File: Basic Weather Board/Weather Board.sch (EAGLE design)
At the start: 4 parts, among them U1 AT30TS75, U2 TMP101", U3 LPS331AP, U4 MPL3115A2

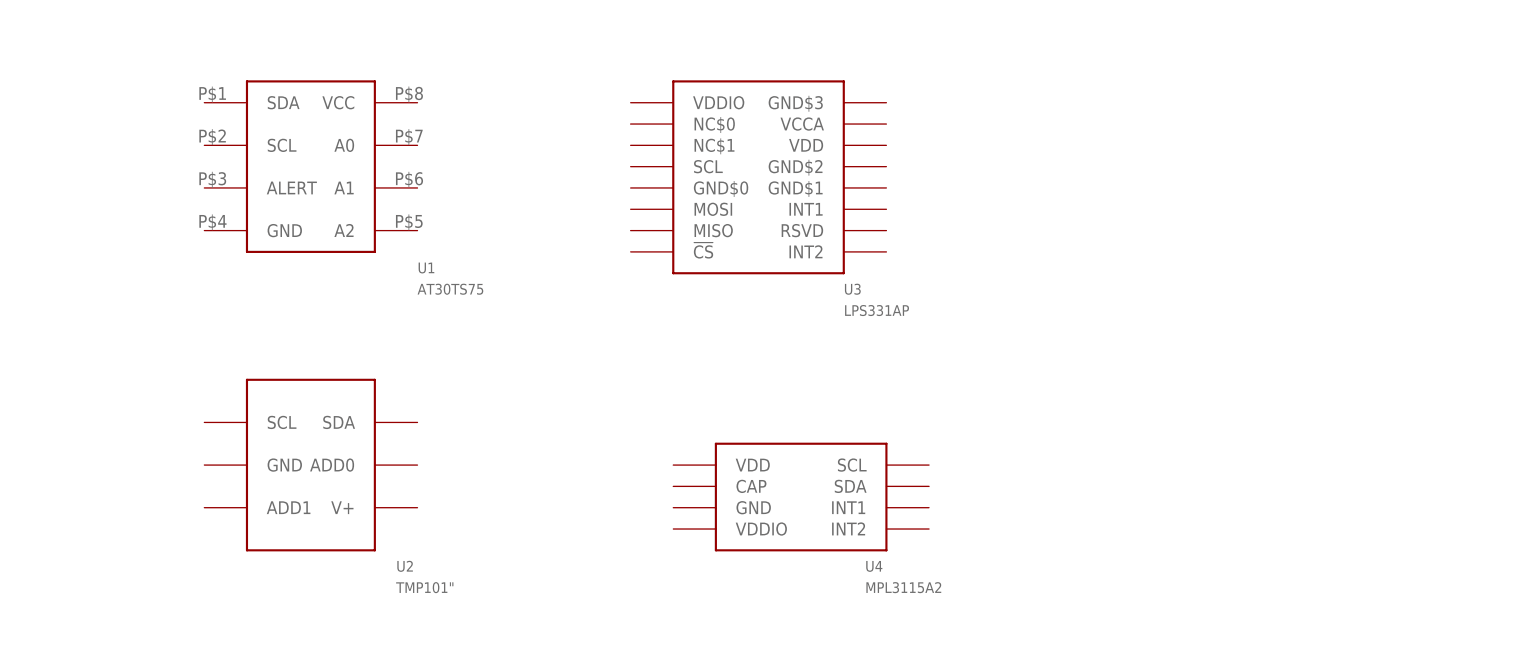
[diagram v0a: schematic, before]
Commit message: FRDM-KL25Z: Corrected parts to use Newark approved components and added missing componnets
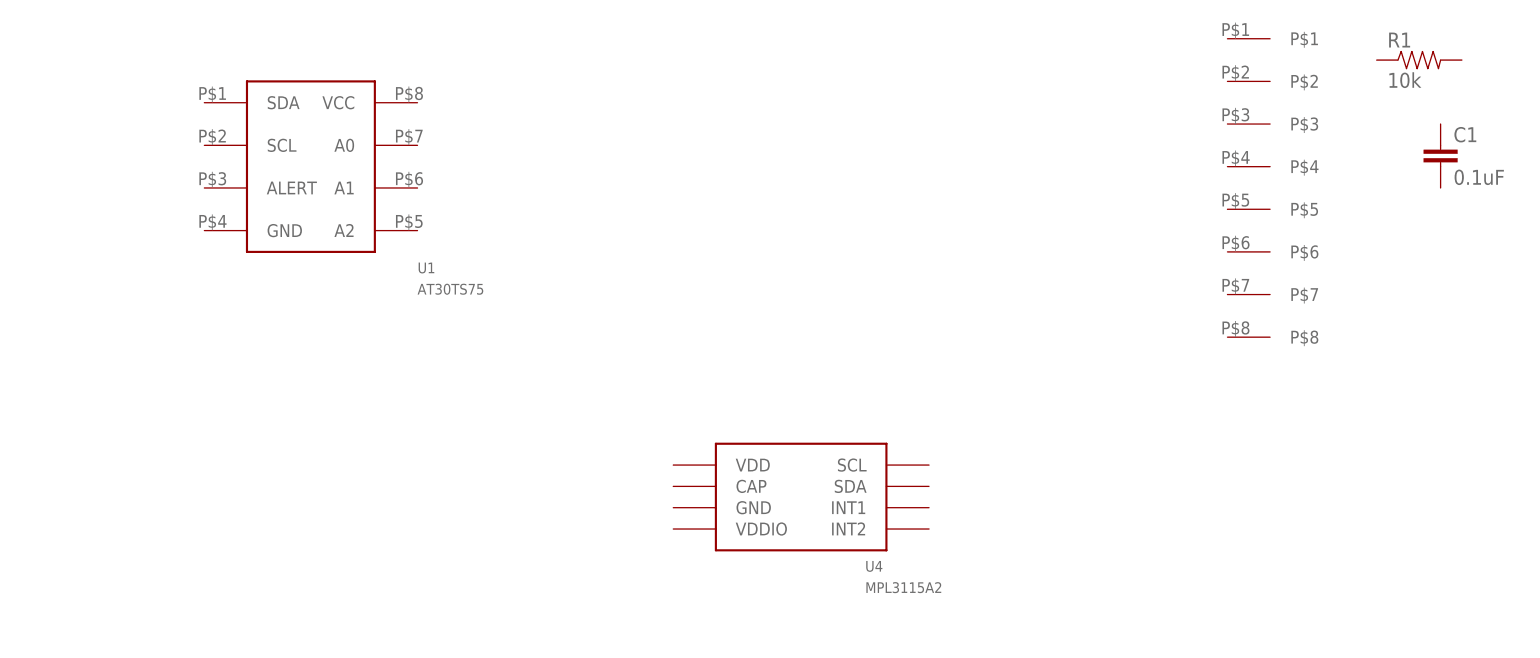
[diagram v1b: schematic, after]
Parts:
- removed U2: TMP101", Kas-Sensors:TMP101"
- removed U3: LPS331AP, Kas-Sensors:LPS331AP
- added C1: 0.1uF, Kas-Capacitors:CAPACITOR0.01U-X7R-10%-25V-0603
- added R1: 10k, Kas-Resistors:RESISTOR10K-63M-1%-50V
- added U$1: STCN75DS2F, Kas-Sensors:STCN75DS2F
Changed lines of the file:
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@@
 <layers>
 <layer number="1" name="Top" color="4" fill="1" visible="no" active="no"/>
+<layer number="2" name="Route2" color="1" fill="3" visible="no" active="no"/>
+<layer number="3" name="Route3" color="4" fill="3" visible="no" active="no"/>
+<layer number="4" name="Route4" color="1" fill="4" visible="no" active="no"/>
+<layer number="5" name="Route5" color="4" fill="4" visible="no" active="no"/>
+<layer number="6" name="Route6" color="1" fill="8" visible="no" active="no"/>
+<layer number="7" name="Route7" color="4" fill="8" visible="no" active="no"/>
+<layer number="8" name="Route8" color="1" fill="2" visible="no" active="no"/>
+<layer number="9" name="Route9" color="4" fill="2" visible="no" active="no"/>
+<layer number="10" name="Route10" color="1" fill="7" visible="no" active="no"/>
+<layer number="11" name="Route11" color="4" fill="7" visible="no" active="no"/>
+<layer number="12" name="Route12" color="1" fill="5" visible="no" active="no"/>
+<layer number="13" name="Route13" color="4" fill="5" visible="no" active="no"/>
+<layer number="14" name="Route14" color="1" fill="6" visible="no" active="no"/>
+<layer number="15" name="Route15" color="4" fill="6" visible="no" active="no"/>
 <layer number="16" name="Bottom" color="1" fill="1" visible="no" active="no"/>
 <layer number="17" name="Pads" color="2" fill="1" visible="no" active="no"/>
@@
 <layer number="48" name="Document" color="7" fill="1" visible="no" active="no"/>
 <layer number="49" name="Reference" color="7" fill="1" visible="no" active="no"/>
+<layer number="50" name="dxf" color="7" fill="1" visible="no" active="no"/>
 <layer number="51" name="tDocu" color="14" fill="1" visible="no" active="no"/>
 <layer number="52" name="bDocu" color="7" fill="1" visible="no" active="no"/>
+<layer number="53" name="tGND_GNDA" color="7" fill="9" visible="no" active="no"/>
+<layer number="54" name="bGND_GNDA" color="1" fill="9" visible="no" active="no"/>
+<layer number="56" name="wert" color="7" fill="1" visible="no" active="no"/>
 <layer number="91" name="Nets" color="2" fill="1" visible="yes" active="yes"/>
 <layer number="92" name="Busses" color="1" fill="1" visible="yes" active="yes"/>
@@
 <layer number="97" name="Info" color="7" fill="1" visible="yes" active="yes"/>
 <layer number="98" name="Guide" color="6" fill="1" visible="yes" active="yes"/>
+<layer number="100" name="Muster" color="7" fill="1" visible="no" active="no"/>
+<layer number="101" name="Patch_Top" color="12" fill="4" visible="no" active="yes"/>
+<layer number="102" name="Vscore" color="7" fill="1" visible="no" active="yes"/>
+<layer number="103" name="tMap" color="7" fill="1" visible="no" active="yes"/>
+<layer number="104" name="Name" color="16" fill="1" visible="no" active="yes"/>
+<layer number="105" name="tPlate" color="7" fill="1" visible="no" active="yes"/>
+<layer number="106" name="bPlate" color="7" fill="1" visible="no" active="yes"/>
+<layer number="107" name="Crop" color="7" fill="1" visible="no" active="yes"/>
+<layer number="116" name="Patch_BOT" color="9" fill="4" visible="no" active="yes"/>
+<layer number="121" name="_tsilk" color="7" fill="1" visible="no" active="yes"/>
+<layer number="122" name="_bsilk" color="7" fill="1" visible="no" active="yes"/>
+<layer number="125" name="_tNames" color="7" fill="1" visible="no" active="yes"/>
+<layer number="144" name="Drill_legend" color="7" fill="1" visible="no" active="yes"/>
+<layer number="151" name="HeatSink" color="7" fill="1" visible="no" active="yes"/>
+<layer number="200" name="200bmp" color="1" fill="10" visible="no" active="yes"/>
+<layer number="201" name="201bmp" color="2" fill="10" visible="no" active="yes"/>
+<layer number="202" name="202bmp" color="3" fill="10" visible="no" active="yes"/>
+<layer number="203" name="203bmp" color="4" fill="10" visible="no" active="yes"/>
+<layer number="204" name="204bmp" color="5" fill="10" visible="no" active="yes"/>
+<layer number="205" name="205bmp" color="6" fill="10" visible="no" active="yes"/>
+<layer number="206" name="206bmp" color="7" fill="10" visible="no" active="yes"/>
+<layer number="207" name="207bmp" color="8" fill="10" visible="no" active="yes"/>
+<layer number="208" name="208bmp" color="9" fill="10" visible="no" active="yes"/>
+<layer number="209" name="209bmp" color="7" fill="1" visible="no" active="yes"/>
+<layer number="210" name="210bmp" color="7" fill="1" visible="no" active="yes"/>
+<layer number="211" name="211bmp" color="7" fill="1" visible="no" active="yes"/>
+<layer number="212" name="212bmp" color="7" fill="1" visible="no" active="yes"/>
+<layer number="213" name="213bmp" color="7" fill="1" visible="no" active="yes"/>
+<layer number="214" name="214bmp" color="7" fill="1" visible="no" active="yes"/>
+<layer number="215" name="215bmp" color="7" fill="1" visible="no" active="yes"/>
+<layer number="216" name="216bmp" color="7" fill="1" visible="no" active="yes"/>
+<layer number="217" name="217bmp" color="18" fill="1" visible="no" active="no"/>
+<layer number="218" name="218bmp" color="19" fill="1" visible="no" active="no"/>
+<layer number="219" name="219bmp" color="20" fill="1" visible="no" active="no"/>
+<layer number="220" name="220bmp" color="21" fill="1" visible="no" active="no"/>
+<layer number="221" name="221bmp" color="22" fill="1" visible="no" active="no"/>
+<layer number="222" name="222bmp" color="23" fill="1" visible="no" active="no"/>
+<layer number="223" name="223bmp" color="24" fill="1" visible="no" active="no"/>
+<layer number="224" name="224bmp" color="25" fill="1" visible="no" active="no"/>
+<layer number="250" name="Descript" color="3" fill="1" visible="no" active="no"/>
+<layer number="251" name="SMDround" color="12" fill="11" visible="no" active="no"/>
+<layer number="254" name="cooling" color="7" fill="1" visible="no" active="yes"/>
 </layers>
 <schematic xreflabel="%F%N/%S.%C%R" xrefpart="/%S.%C%R">
@@
 <parts>
 <part name="U1" library="Kas-Sensors" deviceset="AT30TS75" device=""/>
-<part name="U2" library="Kas-Sensors" deviceset="TMP101" device="&quot;"/>
-<part name="U3" library="Kas-Sensors" deviceset="LPS331AP" device=""/>
 <part name="U4" library="Kas-Sensors" deviceset="MPL3115A2" device=""/>
+<part name="U$1" library="Kas-Sensors" deviceset="STCN75DS2F" device=""/>
+<part name="R1" library="Kas-Resistors" deviceset="RESISTOR" device="10K-63M-1%-50V" value="10k"/>
+<part name="C1" library="Kas-Capacitors" deviceset="CAPACITOR" device="0.01U-X7R-10%-25V-0603" value="0.1uF"/>
 </parts>
 <sheets>
@@
 <instances>
 <instance part="U1" gate="G$1" x="20.32" y="76.2"/>
-<instance part="U2" gate="G$1" x="20.32" y="40.64"/>
-<instance part="U3" gate="G$1" x="73.66" y="76.2"/>
 <instance part="U4" gate="G$1" x="78.74" y="38.1"/>
+<instance part="U$1" gate="G$1" x="137.16" y="86.36"/>
+<instance part="R1" gate="G$1" x="152.4" y="88.9"/>
+<instance part="C1" gate="G$1" x="154.94" y="76.2"/>
 </instances>
 <busses>

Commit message: Weather Board Basic: Minor changes
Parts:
- added C2, C3: 0.1uF, Kas-Capacitors:CAPACITOR0.1U-X7R-10%-10V
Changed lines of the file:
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@@
 <part name="R1" library="Kas-Resistors" deviceset="RESISTOR" device="10K-63M-1%-50V" value="10k"/>
 <part name="C1" library="Kas-Capacitors" deviceset="CAPACITOR" device="0.01U-X7R-10%-25V-0603" value="0.1uF"/>
+<part name="C2" library="Kas-Capacitors" deviceset="CAPACITOR" device="0.1U-X7R-10%-10V" value="0.1uF"/>
+<part name="C3" library="Kas-Capacitors" deviceset="CAPACITOR" device="0.1U-X7R-10%-10V" value="0.1uF"/>
 </parts>
 <sheets>
@@
 <instance part="R1" gate="G$1" x="152.4" y="88.9"/>
 <instance part="C1" gate="G$1" x="154.94" y="76.2"/>
+<instance part="C2" gate="G$1" x="-12.7" y="22.86"/>
+<instance part="C3" gate="G$1" x="-2.54" y="22.86"/>
 </instances>
 <busses>
